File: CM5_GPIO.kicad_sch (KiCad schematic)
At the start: 18 parts, among them J14 Micro_SD_Card_Det, J4 JST_SHBM04B-SRSS-TB, J5 THD-20-R, J9 RJMG201K21120FR, SW1 Right angle Tact button, SW2 SW_DIP_x04, U1 74LVC1G07SE-7, U9 RT9742GGJ5

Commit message: change cad data
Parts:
- C135: renamed from C113; footprint Capacitor_SMD:C_0402_1005Metric -> Capacitor_SMD:C_0402_1005Metric_Pad0.74x0.62mm_HandSolder
- D1, D2: footprint LED_SMD:LED_0603_1608Metric -> LED_SMD:LED_0603_1608Metric_Pad1.05x0.95mm_HandSolder
- renumbered C1 to C4, R8 to R18, R9 to R19, U9 to U3
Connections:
- net BT_nDis: now also SW2.5
- net PMIC_ENABLE: no longer SW2.6
- net PWR_BUT: no longer SW2.5
- net WL_nDis: now also SW2.6
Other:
- moved on the sheet: BT301, C4, D2, J4, R1, SW1, SW2, U1

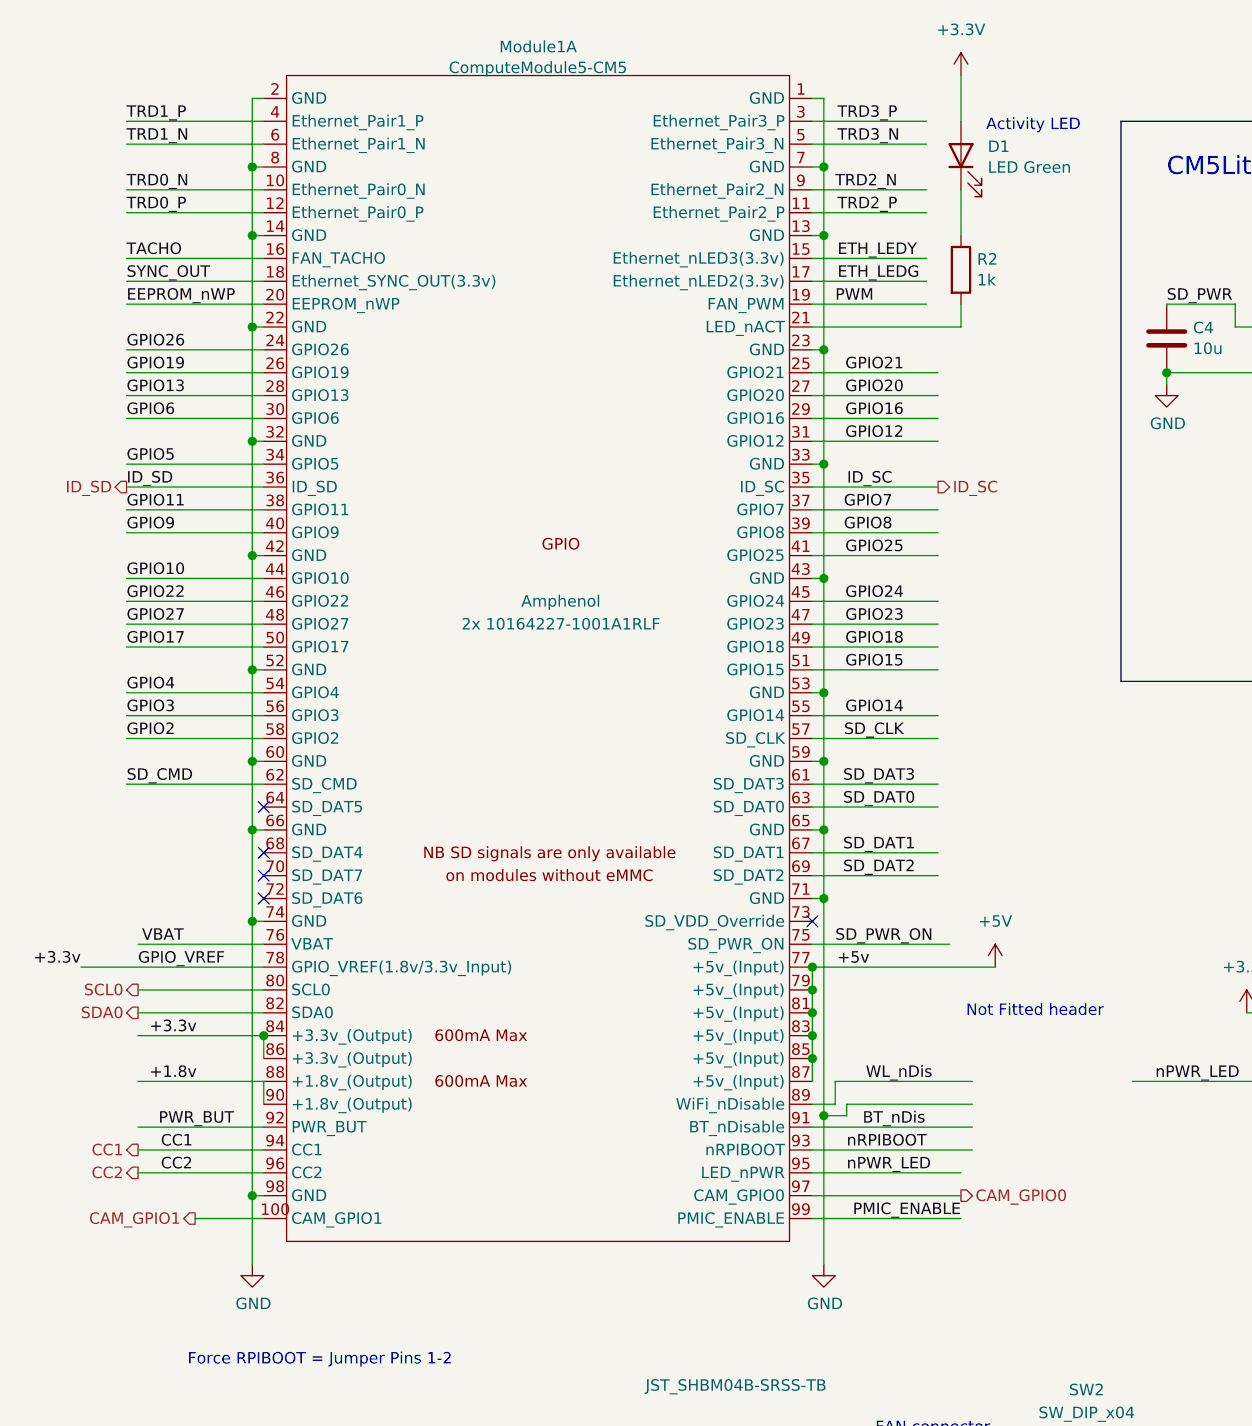
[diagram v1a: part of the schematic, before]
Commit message: change clearance
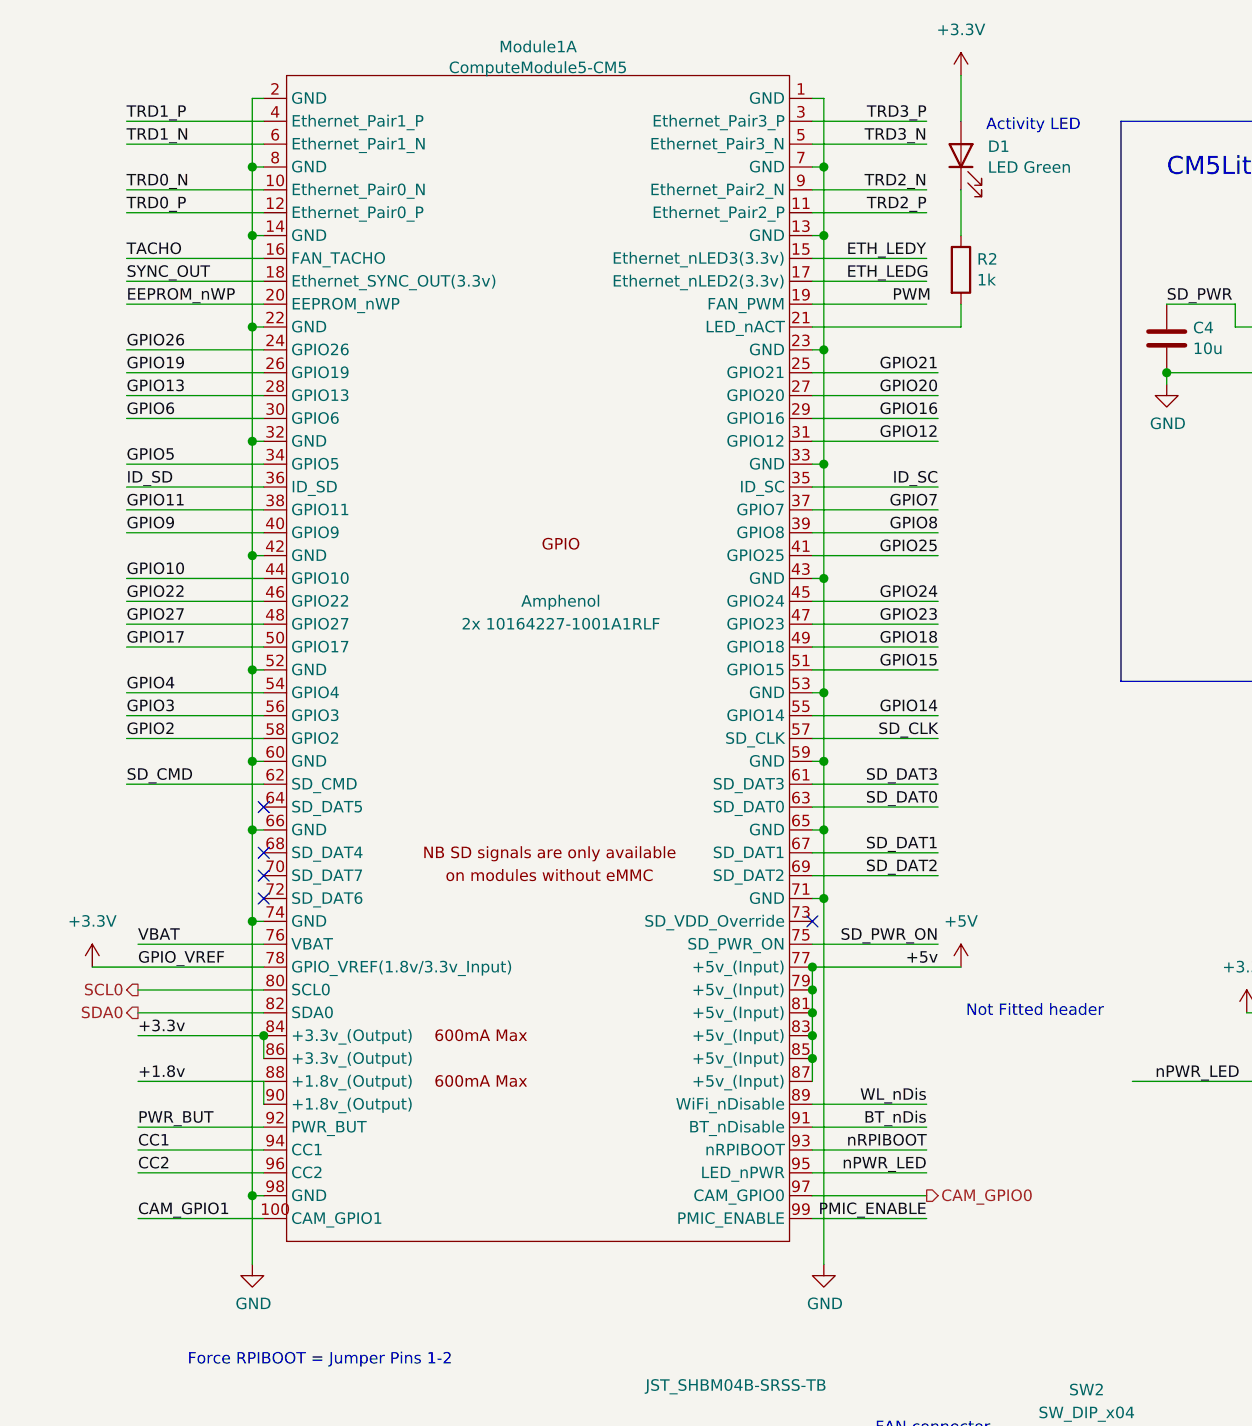
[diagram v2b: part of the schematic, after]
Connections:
- net +3.3V: now also Module1.78 (GPIO_VREF(1.8v/3.3v_Input))
- net +3.3v: no longer Module1.78 (GPIO_VREF(1.8v/3.3v_Input))
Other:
- company: Copyright © 2024 Raspberry Pi Ltd. -> (none)
- title: Compute Module 5 IO Board - GPIO - Ethernet -> (none)

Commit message: change efuse
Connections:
- net +3.3V: no longer Module1.78 (GPIO_VREF(1.8v/3.3v_Input))
- net +3.3v: now also Module1.78 (GPIO_VREF(1.8v/3.3v_Input))
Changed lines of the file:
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@@
 	(wire
 		(pts
-			(xy 20.32 118.11) (xy 39.37 118.11)
+			(xy 25.4 118.11) (xy 39.37 118.11)
 		)
 		(stroke
@@
 		)
 	)
+	(label "+3.3v"
+		(at 25.4 118.11 0)
+		(fields_autoplaced yes)
+		(effects
+			(font
+				(size 1.27 1.27)
+			)
+			(justify left bottom)
+		)
+	)
 	(label "ETH_LEDG"
 		(at 104.14 41.91 0)
@@
 		)
 	)
-	(label "GPIO_VREF"
-		(at 25.4 118.11 0)
-		(fields_autoplaced yes)
-		(effects
-			(font
-				(size 1.27 1.27)
-			)
-			(justify left bottom)
-		)
-	)
 	(label "SD_PWR"
 		(at 139.7 44.45 0)
@@
 					(unit 1)
 				)
-			)
-		)
-	)
-	(symbol
-		(lib_id "power:+3.3V")
-		(at 20.32 118.11 0)
-		(unit 1)
-		(exclude_from_sim no)
-		(in_bom yes)
-		(on_board yes)
-		(dnp no)
-		(fields_autoplaced yes)
-		(property "Reference" "#PWR083"
-			(at 20.32 121.92 0)
-			(effects
-				(font
-					(size 1.27 1.27)
-				)
-				(hide yes)
-			)
-		)
-		(property "Value" "+3.3V"
-			(at 20.32 113.03 0)
-			(effects
-				(font
-					(size 1.27 1.27)
-				)
-			)
-		)
-		(property "Footprint" ""
-			(at 20.32 118.11 0)
-			(effects
-				(font
-					(size 1.27 1.27)
-				)
-				(hide yes)
-			)
-		)
-		(property "Datasheet" ""
-			(at 20.32 118.11 0)
-			(effects
-				(font
-					(size 1.27 1.27)
-				)
-				(hide yes)
-			)
-		)
-		(property "Description" "Power symbol creates a global label with name \"+3.3V\""
-			(at 20.32 118.11 0)
-			(effects
-				(font
-					(size 1.27 1.27)
-				)
-				(hide yes)
-			)
-		)
-		(pin "1"
-		)
-		(instances
-			(project "mainboard4"
-				(path "/dd07ab80-a59c-44f4-ac7d-849e21e1384e/92b565bf-b0e5-4fdf-876c-4b44381d5705"
-					(reference "#PWR083")
-					(unit 1)
-				)

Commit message: remove efuse
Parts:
- renumbered C135 to C125, C4 to C2
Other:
- note added: "SDCARD"
- note removed: "CM5Lite SDCARD I/F"
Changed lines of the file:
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@@
 		)
 	)
-	(text "CM5Lite SDCARD I/F"
+	(text "SDCARD"
 		(exclude_from_sim no)
-		(at 139.7 30.48 0)
+		(at 136.906 28.956 0)
 		(effects
 			(font
@@
 		(on_board yes)
 		(dnp no)
-		(property "Reference" "C4"
+		(property "Reference" "C2"
 			(at 142.621 47.0916 0)
 			(effects
@@
 			(project "CM5IO"
 				(path "/dd07ab80-a59c-44f4-ac7d-849e21e1384e/92b565bf-b0e5-4fdf-876c-4b44381d5705"
-					(reference "C4")
+					(reference "C2")
 					(unit 1)
 				)
@@
 		(on_board yes)
 		(dnp no)
-		(property "Reference" "C135"
+		(property "Reference" "C125"
 			(at 197.231 102.9716 0)
 			(effects
@@
 			(project "mainboard4"
 				(path "/dd07ab80-a59c-44f4-ac7d-849e21e1384e/92b565bf-b0e5-4fdf-876c-4b44381d5705"
-					(reference "C135")
+					(reference "C125")
 					(unit 1)
 				)

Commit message: add sata capacitor
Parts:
- renumbered C125 to C135, C2 to C4, D2 to D1, D1 to D2

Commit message: add logo
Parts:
- Module1: value ComputeModule5-CM5 -> Compute Module 5
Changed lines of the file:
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@@
 			)
 		)
-		(property "Value" "ComputeModule5-CM5"
+		(property "Value" "Compute Module 5"
 			(at 69.85 18.1864 0)
 			(effects

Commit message: add logp
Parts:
- renumbered R18 to R15, R19 to R16
